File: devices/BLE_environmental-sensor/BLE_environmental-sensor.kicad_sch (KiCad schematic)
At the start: 16 parts, among them J1 Conn_02x05_Odd_Even, Q1 Q_PMOS_GSD, U1 BGM220SC12WGA2R, U2 SHT4x, U3 STCC4, U4 LPS22DF, U5 TPS61291DVR, Y1 32.768kHz

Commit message: Finsihes version A.0 of the BLE sensor
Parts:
- removed Q1: Q_PMOS_GSD, Package_TO_SOT_SMD:TSOT-23, symbol Transistor_FET:Q_PMOS_GSD
- removed U1: BGM220SC12WGA2R, custom:SiliconLab_BGM220SC12WGA2R, symbol custom:BGM220SC12WGA2R
- removed Y1: 32.768kHz, Crystal:Crystal_SMD_3215-2Pin_3.2x1.5mm, symbol Device:Crystal
- added C6: 100u, Capacitor_SMD:C_1206_3216Metric, symbol Device:C
- added C7: 100n, Capacitor_SMD:C_0603_1608Metric, symbol Device:C
- added R2, R4: 10k, Resistor_SMD:R_0603_1608Metric, symbol Device:R
- added R3: 1M, Resistor_SMD:R_0603_1608Metric, symbol Device:R
- added TP1, TP2, TP3, TP4, TP5, TP6: RCUCTE, custom:RCUCTE, symbol Connector:TestPoint
- added U1: BGM220PC22HNA2, custom:SiliconLab_BGM220P, symbol custom:BGM220PC22HNA2
- added U6: MX25R8035FM1IL0, Package_SO:JEITA_SOIC-8_3.9x4.9mm_P1.27mm, symbol Memory_Flash:MX25R3235FM1xx0
- BT1: footprint custom:BatteryHolder_MPD_BK-912 -> custom:BatteryHolder_TE_BAT-HLD-001; MPN (none) -> BAT-HLD-001
- C3, C4, C5: MPN (none) -> CL10B104KB8NNNC
- J1: value Conn_02x05_Odd_Even -> Samtec FTSM; footprint (none) -> Connector:Tag-Connect_TC2050-IDC-NL_2x05_P1.27mm_Vertical; MPN (none) -> TC2050-IDC-NL
- R1: value 0 -> 10k; footprint Resistor_SMD:R_01005_0402Metric -> Resistor_SMD:R_0603_1608Metric; MPN (none) -> RC0603FR-0710KL
- U2: MPN (none) -> SHT41-AD1F-R2
- U3: MPN (none) -> STCC4
- U4: MPN (none) -> LPS22DFTR
- U5: footprint (none) -> Package_SON:WSON-6-1EP_2x2mm_P0.65mm_EP1x1.6mm_ThermalVias
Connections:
- net VBAT is gone; now on net VDD: BT1.1 (+)
- net +3.3V: now also TP3.1
- net 3V3_EN: now also R4.1, U1.4 (PB02)
- net GND: now also U4.5 (SA0), U5.7 (GND), C6.2, C7.2, R4.2, TP2.1, U1.1 (GND), U1.12 (GND), U1.20 (GND), U1.31 (GND), U6.4 (GND)
- net PTI_DATA: now also U1.26 (PC04/PTI_DATA)
- net PTI_FRAME: now also U1.27 (PC05/PTI_FRAME)
- net SCL: now also R1.2, U3.1 (SCL), U4.2 (SCL), TP5.1, U1.3 (PB03)
- net SDA: now also U3.5 (SDA), U4.4 (SDA), R2.2, TP4.1, U1.2 (PB04)
- net SWCLK: now also U1.8 (PA01/SWCLK)
- net SWDIO: now also U1.9 (PA02/SWDIO)
- net SWO: now also U1.10 (PA03/SWO)
- net VDD: now also R1.1, C6.1, C7.1, R2.1, R3.1, TP1.1, U1.13 (VDD), U6.3 (~{WP}/SIO2), U6.8 (VCC)
- net DT_READY: now reaches U4.7 (INT_DRDY)
- net DT_READY: now also TP6.1, U1.5 (PB01)
- net SW: now reaches L1.2, U5.1 (SW)
- net UART_RX: now reaches J1.4 (Pin_4)
- net UART_RX: now also U1.15 (PA06)
- net UART_TX: now reaches J1.5 (Pin_5)
- net UART_TX: now also U1.14 (PA05)
- new net MISO: U1.24 (PC02), U6.2 (SO/SIO1)
- new net MOSI: U1.22 (PC00), U6.5 (SI/SIO0)
- new net SPI_CLK: U1.23 (PC01), U6.6 (SCLK)
- new net ~{CS}: R3.2, U1.25 (PC03), U6.1 (~{CS})
- no-connect marks 8 -> 5
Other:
- moved on the sheet: BT1, J1

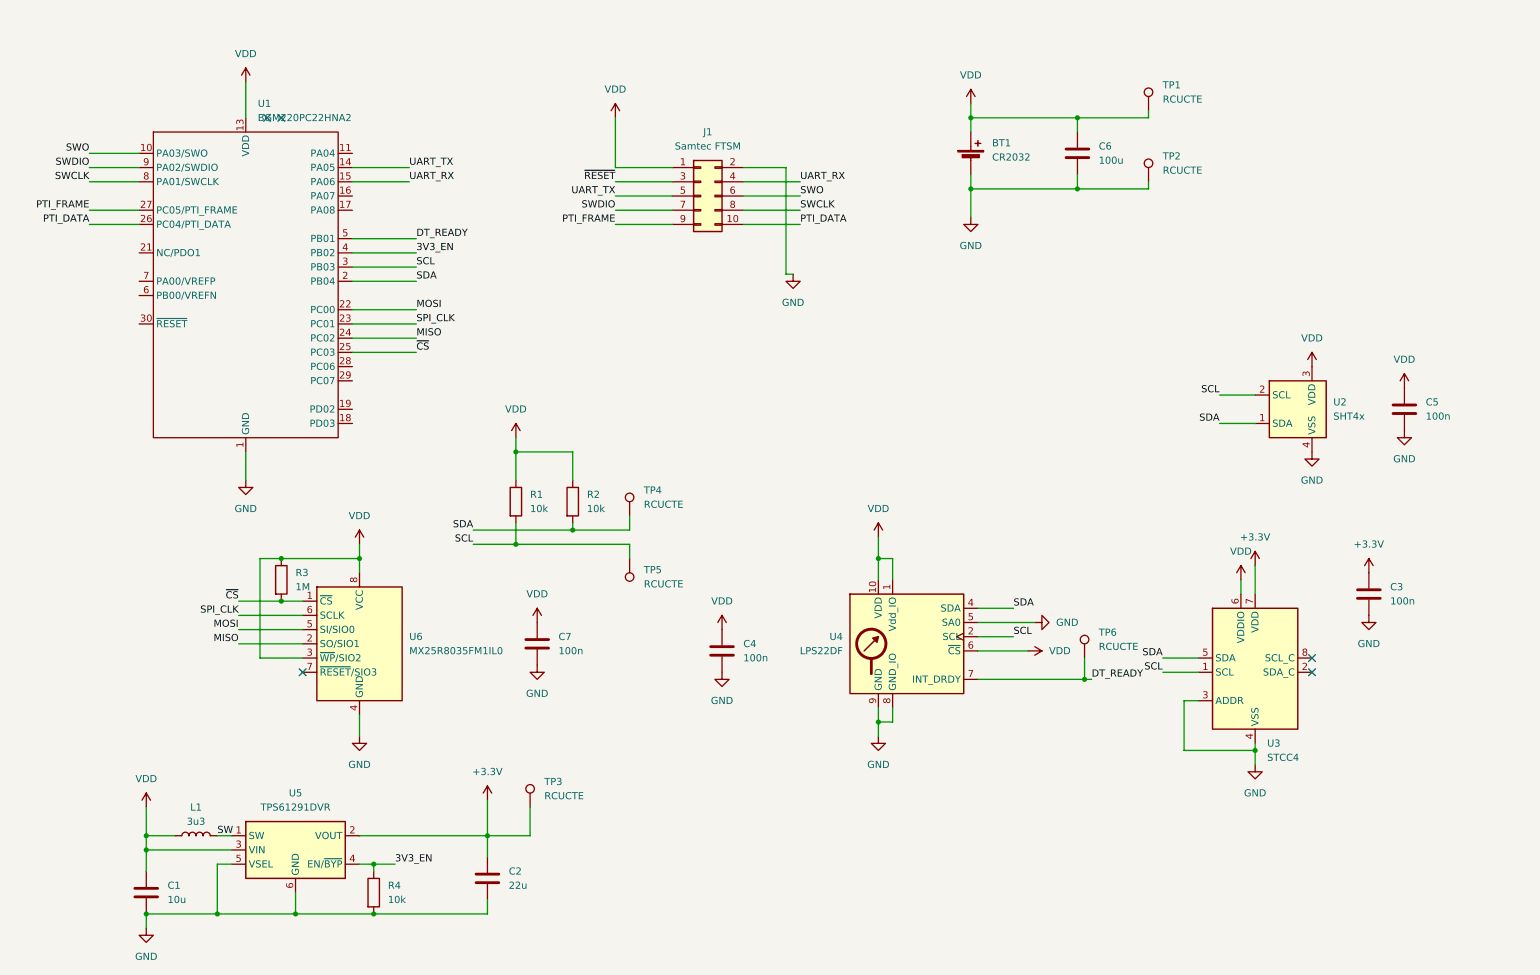
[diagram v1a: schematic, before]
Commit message: Changes the boost converter for the device for better low power performance.
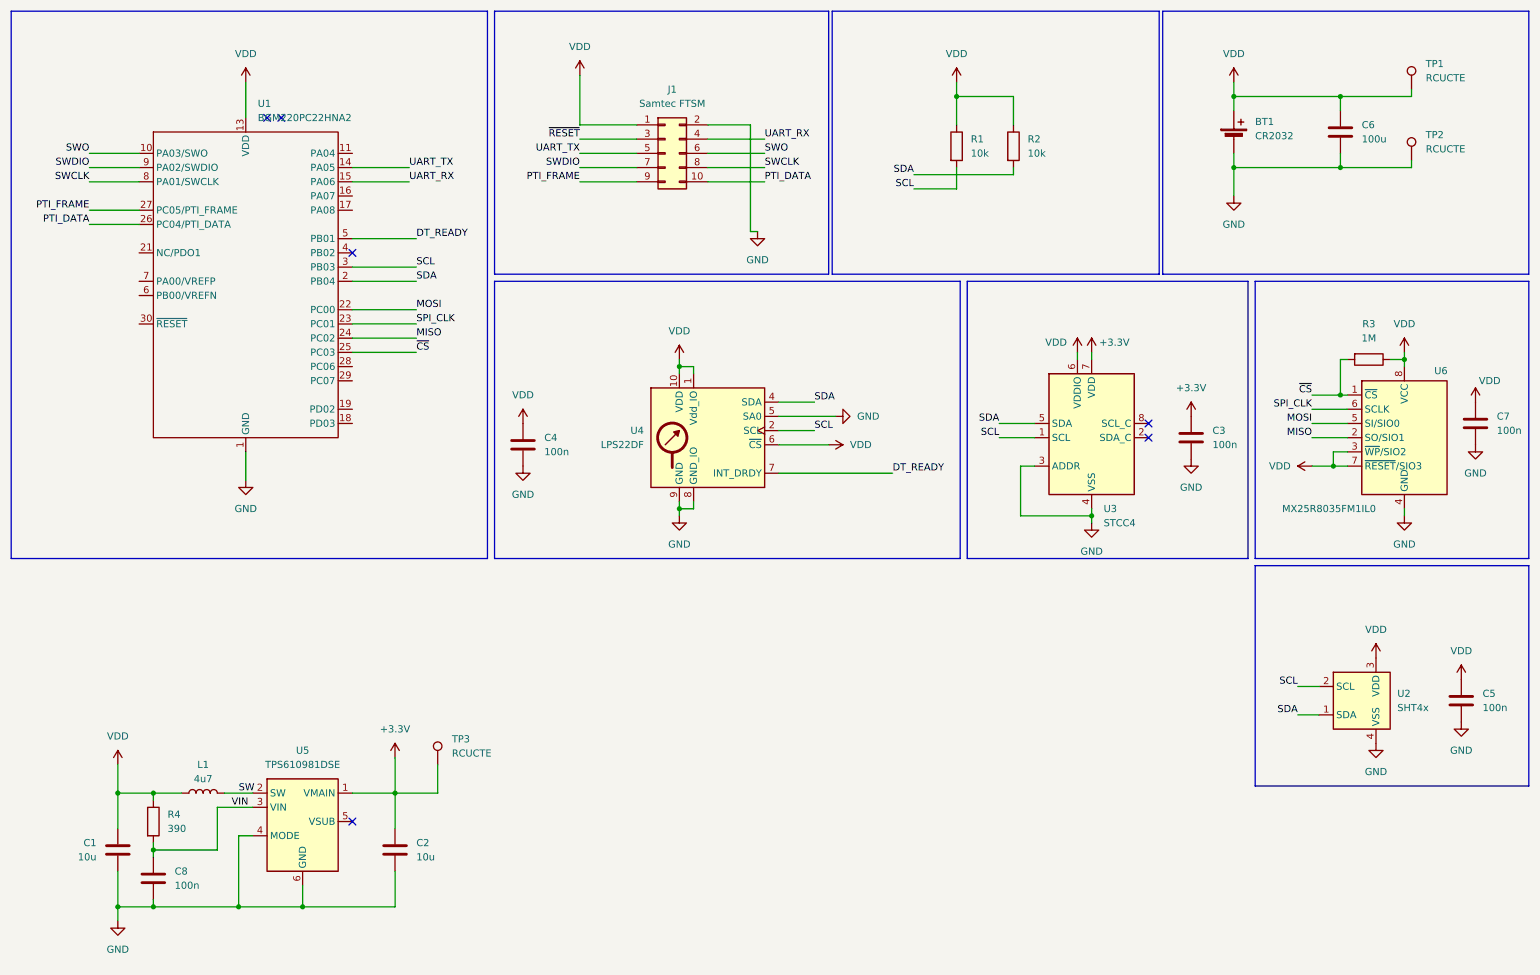
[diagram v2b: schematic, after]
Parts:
- removed TP4, TP5, TP6: RCUCTE, custom:RCUCTE, symbol Connector:TestPoint
- removed U5: TPS61291DVR, Package_SON:WSON-6-1EP_2x2mm_P0.65mm_EP1x1.6mm_ThermalVias, symbol custom:TPS61291DVR
- added C8: 100n, Capacitor_SMD:C_0603_1608Metric, symbol Device:C
- added U5: TPS610981DSE, Package_SON:WSON-6_1.5x1.5mm_P0.5mm, symbol custom:TPS610981DSE
- C2: value 22u -> 10u; MPN GRM21BR60J226ME39L -> GRM219R61A106KE44D
- L1: value 3u3 -> 4u7; footprint Inductor_SMD:L_Taiyo-Yuden_MD-2020 -> custom:L_Bourns-SRN3015; MPN MDMK2020T3R3M -> SRN3015TA-4R7M
- R4: value 10k -> 390; MPN RC0603FR-0710KL -> RC0603FR-07390RL
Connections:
- net +3.3V: now also U5.1 (VMAIN)
- net GND: now also C8.2, U5.4 (MODE), U5.6 (GND); no longer R4.2
- net SW: now also U5.2 (SW)
- net VDD: now also R4.1, U6.7 (~{RESET}/SIO3)
- net 3V3_EN: no longer names the net of U1.4 (PB02)
- net 3V3_EN: no longer R4.1
- new net VIN: C8.1, R4.2, U5.3 (VIN)
- no-connect marks 5 -> 6
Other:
- moved on the sheet: BT1, C1, C3, C4, C5, C6, C7, J1, L1, R1, R2, R3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
